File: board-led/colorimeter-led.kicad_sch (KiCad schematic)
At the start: 2 parts, among them J1 Conn_02x03_Odd_Even

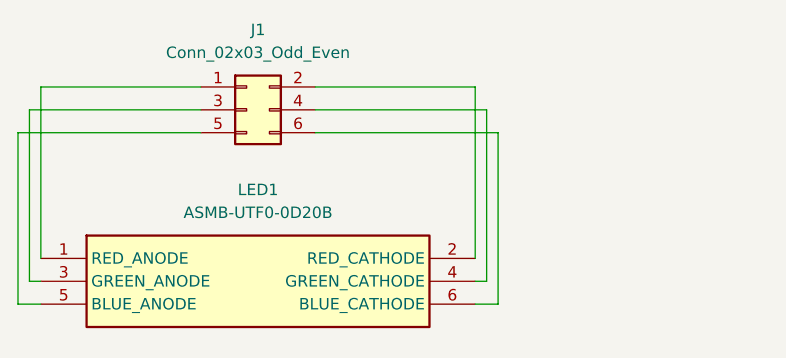
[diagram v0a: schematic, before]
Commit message: Change PD, LED boards to match pinout on main board
Added ground connections to both
Changed Photodiode to have 3x2 connector
Changed LED to common anode
Added new symbol & footprint for common anode RGB LED

Signed-off-by: Ioan Dragomir <ioan.dragomir@analog.com>
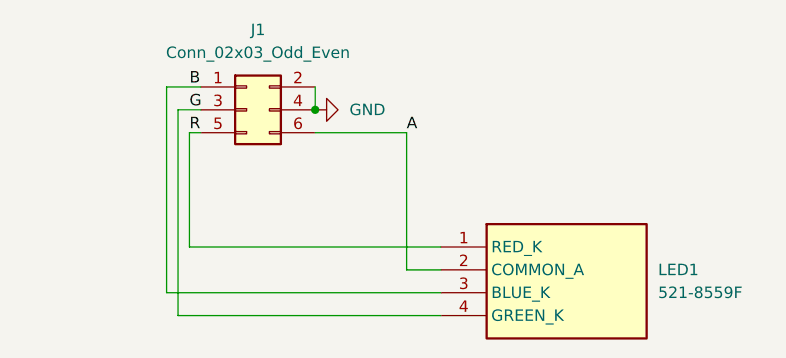
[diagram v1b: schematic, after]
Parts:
- removed LED1: ASMB-UTF0-0D20B, ASMBUTF00D20B, symbol LED:ASMB-UTF0-0D20B
- added LED1: 521-8559F, 5218559F, symbol LED:521-8559F
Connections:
- net B: now reaches J1.1 (Pin_1)
- net B: now also LED1.3 (BLUE_K)
- net GND: now reaches J1.2 (Pin_2)
- net GND: now also J1.4 (Pin_4)
- net G: now reaches J1.3 (Pin_3)
- net G: now also LED1.4 (GREEN_K)
- net R: now reaches J1.5 (Pin_5)
- net R: now also LED1.1 (RED_K)
- net A: now reaches J1.6 (Pin_6)
- net A: now also LED1.2 (COMMON_A)
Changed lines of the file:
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@@
 (kicad_sch (version 20230121) (generator eeschema)
   (paper "A4")
-  (wire (pts (xy 34.29 69.85) (xy 33.02 69.85))
+  (junction (at 64.77 50.8) (diameter 0) (color 0 0 0 0)
+  )
+  (wire (pts (xy 78.74 73.66) (xy 49.53 73.66))
     (stroke (width 0) (type default))
   )
-  (wire (pts (xy 64.77 50.8) (xy 83.82 50.8))
+  (wire (pts (xy 48.26 71.12) (xy 48.26 48.26))
     (stroke (width 0) (type default))
   )
-  (wire (pts (xy 85.09 53.34) (xy 64.77 53.34))
+  (wire (pts (xy 49.53 73.66) (xy 49.53 50.8))
     (stroke (width 0) (type default))
   )
-  (wire (pts (xy 31.75 72.39) (xy 31.75 53.34))
+  (wire (pts (xy 74.93 53.34) (xy 74.93 68.58))
     (stroke (width 0) (type default))
   )
-  (wire (pts (xy 34.29 67.31) (xy 34.29 48.26))
+  (wire (pts (xy 49.53 50.8) (xy 52.07 50.8))
     (stroke (width 0) (type default))
   )
-  (wire (pts (xy 85.09 72.39) (xy 85.09 53.34))
+  (wire (pts (xy 64.77 53.34) (xy 74.93 53.34))
     (stroke (width 0) (type default))
   )
-  (wire (pts (xy 82.55 67.31) (xy 82.55 48.26))
+  (wire (pts (xy 64.77 48.26) (xy 64.77 50.8))
     (stroke (width 0) (type default))
   )
-  (wire (pts (xy 33.02 69.85) (xy 33.02 50.8))
+  (wire (pts (xy 50.8 66.04) (xy 50.8 53.34))
     (stroke (width 0) (type default))
   )
-  (wire (pts (xy 34.29 72.39) (xy 31.75 72.39))
+  (wire (pts (xy 78.74 66.04) (xy 50.8 66.04))
     (stroke (width 0) (type default))
   )
-  (wire (pts (xy 33.02 50.8) (xy 52.07 50.8))
+  (wire (pts (xy 74.93 68.58) (xy 78.74 68.58))
     (stroke (width 0) (type default))
   )
-  (wire (pts (xy 82.55 48.26) (xy 64.77 48.26))
+  (wire (pts (xy 50.8 53.34) (xy 52.07 53.34))
     (stroke (width 0) (type default))
   )
-  (wire (pts (xy 82.55 72.39) (xy 85.09 72.39))
+  (wire (pts (xy 48.26 48.26) (xy 52.07 48.26))
     (stroke (width 0) (type default))
   )
-  (wire (pts (xy 83.82 50.8) (xy 83.82 69.85))
+  (wire (pts (xy 78.74 71.12) (xy 48.26 71.12))
     (stroke (width 0) (type default))
   )
-  (wire (pts (xy 83.82 69.85) (xy 82.55 69.85))
-    (stroke (width 0) (type default))
+  (label "R" (at 50.8 53.34 0) (fields_autoplaced)
+    (effects (font (size 1.27 1.27)) (justify left bottom))
   )
-  (wire (pts (xy 31.75 53.34) (xy 52.07 53.34))
-    (stroke (width 0) (type default))
+  (label "B" (at 50.8 48.26 0) (fields_autoplaced)
+    (effects (font (size 1.27 1.27)) (justify left bottom))
   )
-  (wire (pts (xy 34.29 48.26) (xy 52.07 48.26))
-    (stroke (width 0) (type default))
+  (label "A" (at 74.93 53.34 0) (fields_autoplaced)
+    (effects (font (size 1.27 1.27)) (justify left bottom))
+  )
+  (label "G" (at 50.8 50.8 0) (fields_autoplaced)
+    (effects (font (size 1.27 1.27)) (justify left bottom))
+  )
+  (symbol (lib_id "LED:521-8559F") (at 78.74 66.04 0) (unit 1)
+    (in_bom yes) (on_board yes) (dnp no) (fields_autoplaced)
+    (property "Reference" "LED1" (at 102.87 68.58 0)
+      (effects (font (size 1.27 1.27)) (justify left))
+    )
+    (property "Value" "521-8559F" (at 102.87 71.12 0)
+      (effects (font (size 1.27 1.27)) (justify left))
+    )
+    (property "Footprint" "5218559F" (at 102.87 160.96 0)
+      (effects (font (size 1.27 1.27)) (justify left top) hide)
+    )
+    (property "Datasheet" "" (at 102.87 260.96 0)
+      (effects (font (size 1.27 1.27)) (justify left top) hide)
+    )
+    (property "Height" "8.6" (at 102.87 460.96 0)
+      (effects (font (size 1.27 1.27)) (justify left top) hide)
+    )
+    (property "Mouser Part Number" "645-5218559F" (at 102.87 560.96 0)
+      (effects (font (size 1.27 1.27)) (justify left top) hide)
+    )
+    (property "Mouser Price/Stock" "https://www.mouser.co.uk/ProductDetail/Dialight/521-8559F?qs=vmHwEFxEFR%2FyCJVY9sdZTA%3D%3D" (at 102.87 660.96 0)
+      (effects (font (size 1.27 1.27)) (justify left top) hide)
+    )
+    (property "Manufacturer_Name" "Dialight" (at 102.87 760.96 0)
+      (effects (font (size 1.27 1.27)) (justify left top) hide)
+    )
+    (property "Manufacturer_Part_Number" "521-8559F" (at 102.87 860.96 0)
+      (effects (font (size 1.27 1.27)) (justify left top) hide)
+    )
+    (pin "1")
+    (pin "2")
+    (pin "3")
+    (pin "4")
+    (instances
+      (project "colorimeter-led"
+        (path "/07b84b89-9cb0-4a6c-b42a-5b5a95d67ceb"
+          (reference "LED1") (unit 1)
+        )
+      )
+    )
+  )
+  (symbol (lib_id "power:GND") (at 64.77 50.8 90) (unit 1)
+    (in_bom yes) (on_board yes) (dnp no) (fields_autoplaced)
+    (property "Reference" "#PWR01" (at 71.12 50.8 0)
+      (effects (font (size 1.27 1.27)) hide)
+    )
+    (property "Value" "GND" (at 68.58 50.8 90)
+      (effects (font (size 1.27 1.27)) (justify right))
+    )
+    (property "Footprint" "" (at 64.77 50.8 0)
+      (effects (font (size 1.27 1.27)) hide)
+    )
+    (property "Datasheet" "" (at 64.77 50.8 0)
+      (effects (font (size 1.27 1.27)) hide)
+    )
+    (pin "1")
+    (instances
+      (project "colorimeter-led"
+        (path "/07b84b89-9cb0-4a6c-b42a-5b5a95d67ceb"
+          (reference "#PWR01") (unit 1)
+        )
+      )
+    )
   )
   (symbol (lib_id "Connector_Generic:Conn_02x03_Odd_Even") (at 57.15 50.8 0) (unit 1)
@@
         )
       )
-    )
-  )
-  (symbol (lib_id "LED:ASMB-UTF0-0D20B") (at 34.29 67.31 0) (unit 1)
-    (in_bom yes) (on_board yes) (dnp no) (fields_autoplaced)
-    (property "Reference" "LED1" (at 58.42 59.69 0)
-      (effects (font (size 1.27 1.27)))
-    )
-    (property "Value" "ASMB-UTF0-0D20B" (at 58.42 62.23 0)
-      (effects (font (size 1.27 1.27)))
-    )
-    (property "Footprint" "ASMBUTF00D20B" (at 78.74 64.77 0)
-      (effects (font (size 1.27 1.27)) (justify left) hide)
-    )
-    (property "Datasheet" "https://docs.broadcom.com/docs/ASMB-UTF0-0D20B-DS100" (at 78.74 67.31 0)
-      (effects (font (size 1.27 1.27)) (justify left) hide)
-    )
-    (property "Description" "Standard LEDs - SMD 2828 Tricolor PLCC6 LEDs" (at 78.74 69.85 0)
-      (effects (font (size 1.27 1.27)) (justify left) hide)
-    )
-    (property "Height" "2.6" (at 78.74 72.39 0)
-      (effects (font (size 1.27 1.27)) (justify left) hide)
-    )
-    (property "Mouser Part Number" "630-ASMB-UTF0-0D20B" (at 78.74 74.93 0)
-      (effects (font (size 1.27 1.27)) (justify left) hide)
-    )
-    (property "Mouser Price/Stock" "https://www.mouser.co.uk/ProductDetail/Broadcom-Avago/ASMB-UTF0-0D20B?qs=T3oQrply3y8r8SVYhPt2pg%3D%3D" (at 78.74 77.47 0)
-      (effects (font (size 1.27 1.27)) (justify left) hide)
-    )
-    (property "Manufacturer_Name" "Avago Technologies" (at 78.74 80.01 0)
-      (effects (font (size 1.27 1.27)) (justify left) hide)
-    )
-    (property "Manufacturer_Part_Number" "ASMB-UTF0-0D20B" (at 78.74 82.55 0)
-      (effects (font (size 1.27 1.27)) (justify left) hide)
-    )
-    (pin "1")
-    (pin "2")
-    (pin "3")
-    (pin "4")
-    (pin "5")
-    (pin "6")
-    (instances
-      (project "colorimeter-led"
-        (path "/07b84b89-9cb0-4a6c-b42a-5b5a95d67ceb"
-          (reference "LED1") (unit 1)
-        )
-      )
